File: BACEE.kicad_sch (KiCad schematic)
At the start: 0 parts

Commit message: Created new child sheet, added project symbols
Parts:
- added BT1: Battery, symbol Device:Battery
- added C1, C2: C, symbol Device:C
- added C3, C4: C_Polarized, symbol Device:C_Polarized
- added D1: LED, symbol Device:LED
- added R1, R2: R, symbol Device:R
- added U1: 24LC1025, symbol Memory_EEPROM:24LC1025
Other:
- added sheet Connector (Connectors.kicad_sch)

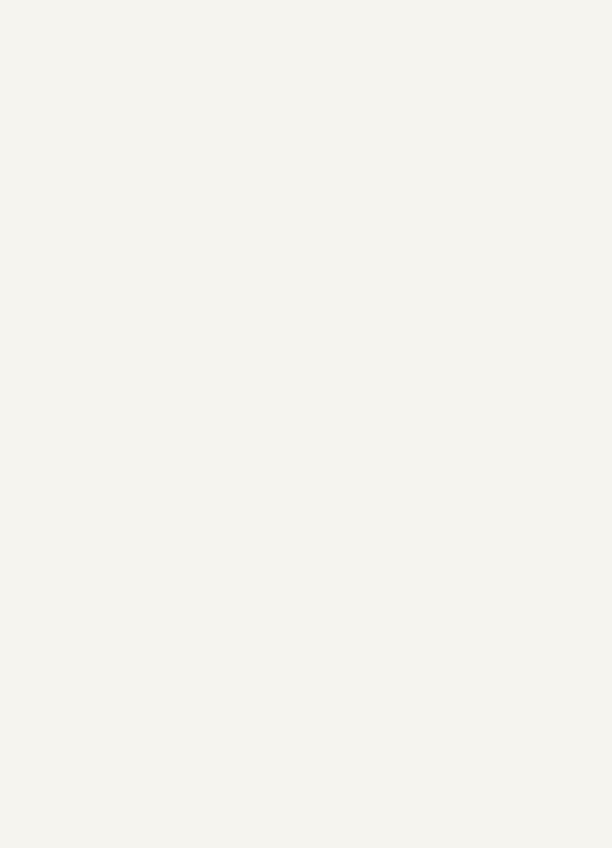
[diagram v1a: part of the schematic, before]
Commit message: Added symbol for ATMEGA328P-AU
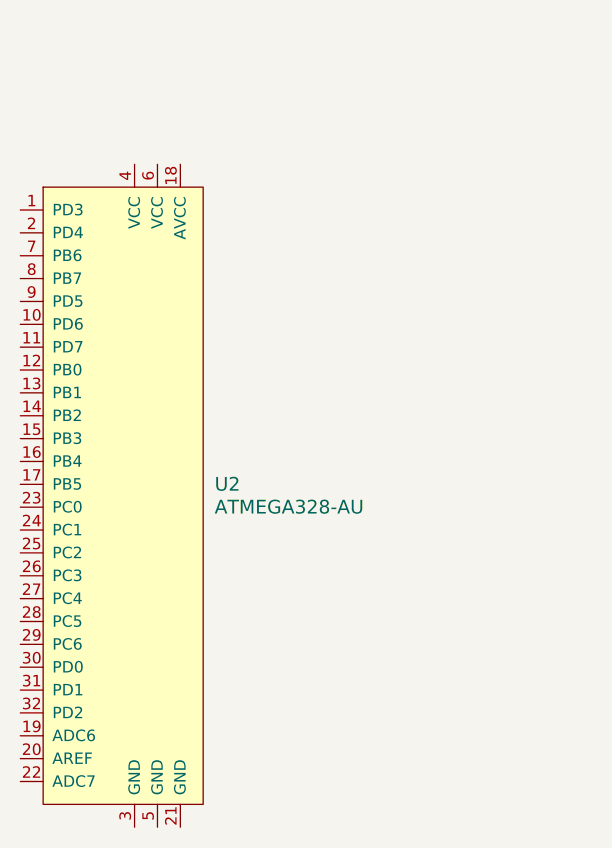
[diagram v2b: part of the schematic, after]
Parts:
- added U2: ATMEGA328-AU, digikey-footprints:TQFP-32_7x7mm, symbol dk_Embedded-Microcontrollers:ATMEGA328-AU
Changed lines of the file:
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@@
+	)
+	(symbol
+		(lib_id "dk_Embedded-Microcontrollers:ATMEGA328-AU")
+		(at 76.2 127 0)
+		(unit 1)
+		(exclude_from_sim no)
+		(in_bom yes)
+		(on_board yes)
+		(dnp no)
+		(fields_autoplaced yes)
+		(property "Reference" "U2"
+			(at 85.09 147.3199 0)
+			(effects
+				(font
+					(size 1.524 1.524)
+				)
+				(justify left)
+			)
+		)
+		(property "Value" "ATMEGA328-AU"
+			(at 85.09 149.8599 0)
+			(effects
+				(font
+					(size 1.524 1.524)
+				)
+				(justify left)
+			)
+		)
+		(property "Footprint" "digikey-footprints:TQFP-32_7x7mm"
+			(at 81.28 121.92 0)
+			(effects
+				(font
+					(size 1.524 1.524)
+				)
+				(justify left)
+				(hide yes)
+			)
+		)
+		(property "Datasheet" "http://www.microchip.com/mymicrochip/filehandler.aspx?ddocname=en608326"
+			(at 81.28 119.38 0)
+			(effects
+				(font
+					(size 1.524 1.524)
+				)
+				(justify left)
+				(hide yes)
+			)
+		)
+		(property "Description" "IC MCU 8BIT 32KB FLASH 32TQFP"
+			(at 76.2 127 0)
+			(effects
+				(font
+					(size 1.27 1.27)
+				)
+				(hide yes)
+			)
+		)
+		(property "Digi-Key_PN" "ATMEGA328-AU-ND"
+			(at 81.28 116.84 0)
+			(effects
+				(font
+					(size 1.524 1.524)
+				)
+				(justify left)
+				(hide yes)
+			)
+		)
+		(property "MPN" "ATMEGA328-AU"
+			(at 81.28 114.3 0)
+			(effects
+				(font
+					(size 1.524 1.524)
+				)
+				(justify left)
+				(hide yes)
+			)
+		)
+		(property "Category" "Integrated Circuits (ICs)"
+			(at 81.28 111.76 0)
+			(effects
+				(font
+					(size 1.524 1.524)
+				)
+				(justify left)
+				(hide yes)
+			)
+		)
+		(property "Family" "Embedded - Microcontrollers"
+			(at 81.28 109.22 0)
+			(effects
+				(font
+					(size 1.524 1.524)
+				)
+				(justify left)
+				(hide yes)
+			)
+		)
+		(property "DK_Datasheet_Link" "http://www.microchip.com/mymicrochip/filehandler.aspx?ddocname=en608326"
+			(at 81.28 106.68 0)
+			(effects
+				(font
+					(size 1.524 1.524)
+				)
+				(justify left)
+				(hide yes)
+			)
+		)
+		(property "DK_Detail_Page" "/product-detail/en/microchip-technology/ATMEGA328-AU/ATMEGA328-AU-ND/2271029"
+			(at 81.28 104.14 0)
+			(effects
+				(font
+					(size 1.524 1.524)
+				)
+				(justify left)
+				(hide yes)
+			)
+		)
+		(property "Description_1" "IC MCU 8BIT 32KB FLASH 32TQFP"
+			(at 81.28 101.6 0)
+			(effects
+				(font
+					(size 1.524 1.524)
+				)
+				(justify left)
+				(hide yes)
+			)
+		)
+		(property "Manufacturer" "Microchip Technology"
+			(at 81.28 99.06 0)
+			(effects
+				(font
+					(size 1.524 1.524)
+				)
+				(justify left)
+				(hide yes)
+			)
+		)
+		(property "Status" "Active"
+			(at 81.28 96.52 0)
+			(effects
+				(font
+					(size 1.524 1.524)
+				)
+				(justify left)
+				(hide yes)
+			)
+		)
+		(pin "15"
+		)
+		(pin "2"
+		)
+		(pin "8"
+		)
+		(pin "25"
+		)
+		(pin "21"
+		)
+		(pin "11"
+		)
+		(pin "9"
+		)
+		(pin "14"
+		)
+		(pin "13"
+		)
+		(pin "12"
+		)
+		(pin "27"
+		)
+		(pin "20"
+		)
+		(pin "17"
+		)
+		(pin "16"
+		)
+		(pin "30"
+		)
+		(pin "22"
+		)
+		(pin "6"
+		)
+		(pin "5"
+		)
+		(pin "23"
+		)
+		(pin "28"
+		)
+		(pin "31"
+		)
+		(pin "32"
+		)
+		(pin "4"
+		)
+		(pin "19"
+		)
+		(pin "10"
+		)
+		(pin "29"
+		)
+		(pin "7"
+		)
+		(pin "26"
+		)
+		(pin "18"
+		)
+		(pin "24"
+		)
+		(pin "1"
+		)
+		(pin "3"
+		)
+		(instances
+			(project ""
+				(path "/6ce24059-c414-47b5-8b66-25e9f97a79bc"
+					(reference "U2")
+					(unit 1)
+				)
+			)
+		)
 	)
 	(symbol

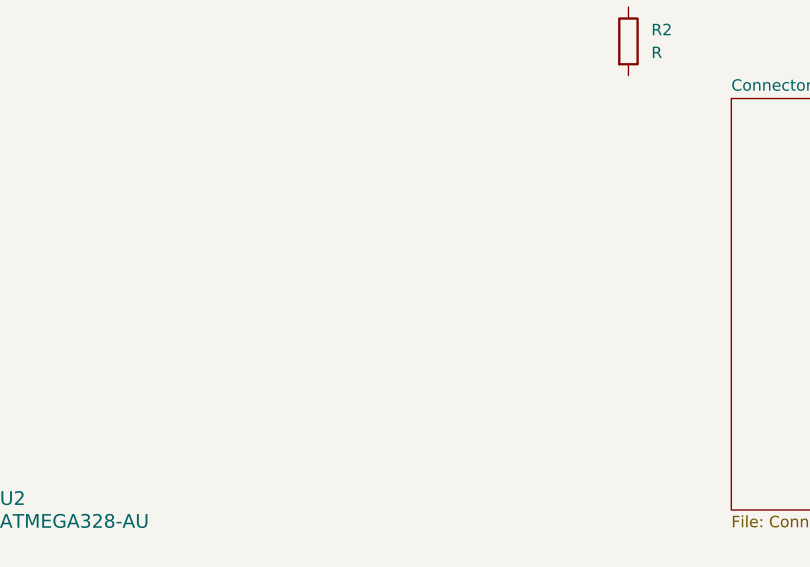
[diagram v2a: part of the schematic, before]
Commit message: Added custom clock IC symbol
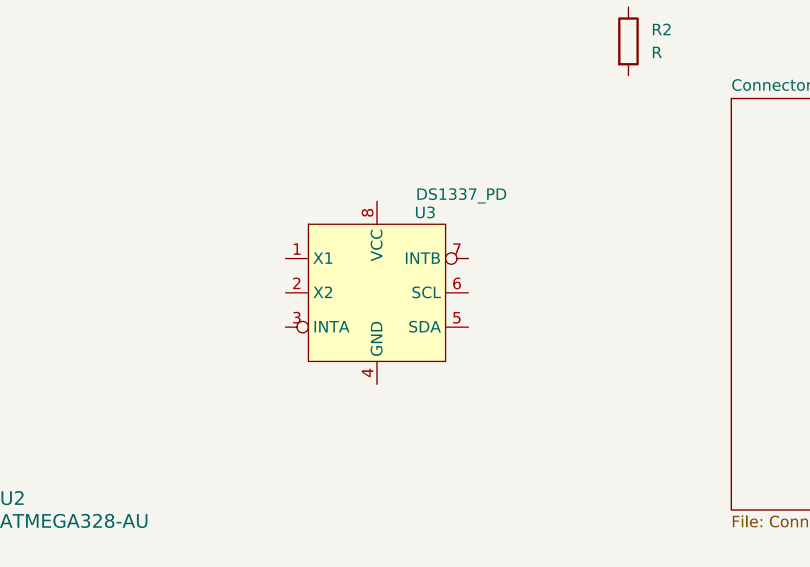
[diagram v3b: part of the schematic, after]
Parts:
- added U3: DS1337_PD, symbol Gathonjia:DS1337_PD
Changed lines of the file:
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@@
+	)
+	(symbol
+		(lib_id "Gathonjia:DS1337_PD")
+		(at 127 124.46 0)
+		(unit 1)
+		(exclude_from_sim no)
+		(in_bom yes)
+		(on_board yes)
+		(dnp no)
+		(property "Reference" "U3"
+			(at 131.1753 115.57 0)
+			(effects
+				(font
+					(size 1.27 1.27)
+				)
+				(justify left)
+			)
+		)
+		(property "Value" "DS1337_PD"
+			(at 131.318 113.538 0)
+			(effects
+				(font
+					(size 1.27 1.27)
+				)
+				(justify left)
+			)
+		)
+		(property "Footprint" ""
+			(at 127 124.46 0)
+			(effects
+				(font
+					(size 1.27 1.27)
+				)
+				(hide yes)
+			)
+		)
+		(property "Datasheet" ""
+			(at 127 124.46 0)
+			(effects
+				(font
+					(size 1.27 1.27)
+				)
+				(hide yes)
+			)
+		)
+		(property "Description" ""
+			(at 127 124.46 0)
+			(effects
+				(font
+					(size 1.27 1.27)
+				)
+				(hide yes)
+			)
+		)
+		(pin "3"
+		)
+		(pin "5"
+		)
+		(pin "8"
+		)
+		(pin "4"
+		)
+		(pin "2"
+		)
+		(pin "1"
+		)
+		(pin "7"
+		)
+		(pin "6"
+		)
+		(instances
+			(project ""
+				(path "/6ce24059-c414-47b5-8b66-25e9f97a79bc"
+					(reference "U3")
+					(unit 1)
+				)
+			)
+		)
 	)
 	(symbol

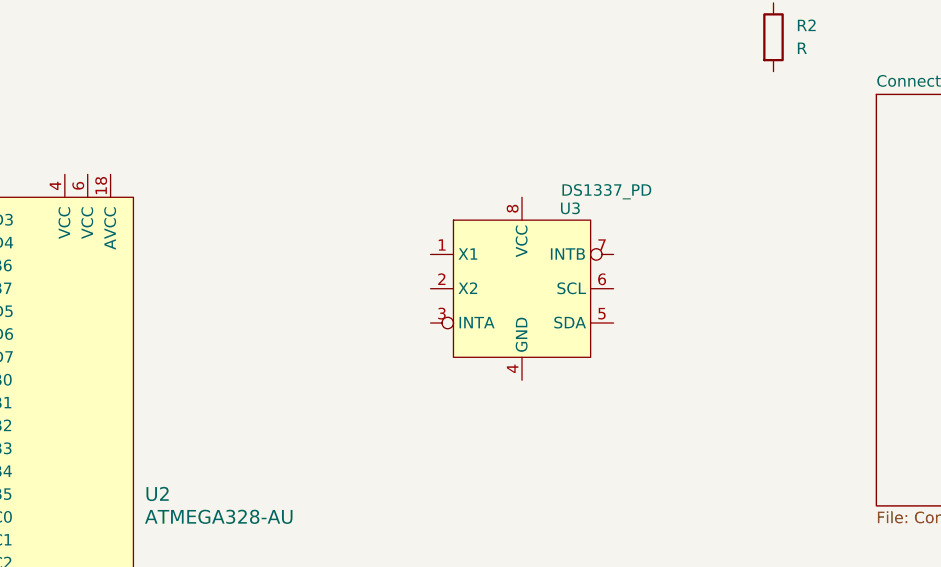
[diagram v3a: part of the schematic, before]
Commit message: Added missing crystals
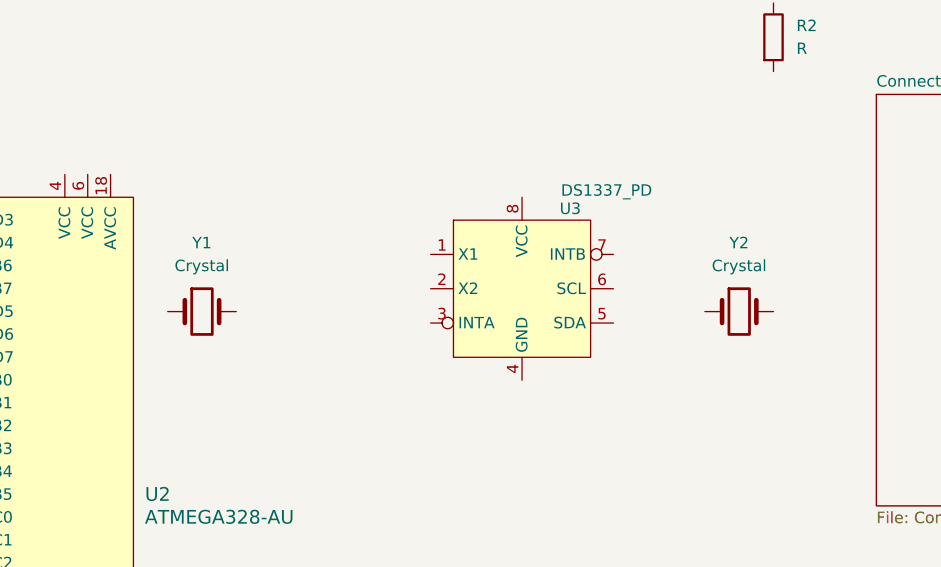
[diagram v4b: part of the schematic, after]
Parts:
- added Y1, Y2: Crystal, symbol Device:Crystal
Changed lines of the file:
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@@
+	)
+	(symbol
+		(lib_id "Device:Crystal")
+		(at 151.13 127 0)
+		(unit 1)
+		(exclude_from_sim no)
+		(in_bom yes)
+		(on_board yes)
+		(dnp no)
+		(fields_autoplaced yes)
+		(property "Reference" "Y2"
+			(at 151.13 119.38 0)
+			(effects
+				(font
+					(size 1.27 1.27)
+				)
+			)
+		)
+		(property "Value" "Crystal"
+			(at 151.13 121.92 0)
+			(effects
+				(font
+					(size 1.27 1.27)
+				)
+			)
+		)
+		(property "Footprint" ""
+			(at 151.13 127 0)
+			(effects
+				(font
+					(size 1.27 1.27)
+				)
+				(hide yes)
+			)
+		)
+		(property "Datasheet" "~"
+			(at 151.13 127 0)
+			(effects
+				(font
+					(size 1.27 1.27)
+				)
+				(hide yes)
+			)
+		)
+		(property "Description" "Two pin crystal"
+			(at 151.13 127 0)
+			(effects
+				(font
+					(size 1.27 1.27)
+				)
+				(hide yes)
+			)
+		)
+		(pin "2"
+		)
+		(pin "1"
+		)
+		(instances
+			(project "BACEE"
+				(path "/6ce24059-c414-47b5-8b66-25e9f97a79bc"
+					(reference "Y2")
+					(unit 1)
+				)
+			)
+		)
 	)
 	(symbol
@@
 					(unit 1)
 				)
+			)
+		)
+	)
+	(symbol
+		(lib_id "Device:Crystal")
+		(at 91.44 127 0)
+		(unit 1)
+		(exclude_from_sim no)
+		(in_bom yes)
+		(on_board yes)
+		(dnp no)
+		(fields_autoplaced yes)
+		(property "Reference" "Y1"
+			(at 91.44 119.38 0)
+			(effects
+				(font
+					(size 1.27 1.27)
+				)
+			)
+		)
+		(property "Value" "Crystal"
+			(at 91.44 121.92 0)
+			(effects
+				(font
+					(size 1.27 1.27)
+				)
+			)
+		)
+		(property "Footprint" ""
+			(at 91.44 127 0)
+			(effects
+				(font
+					(size 1.27 1.27)
+				)
+				(hide yes)
+			)
+		)
+		(property "Datasheet" "~"
+			(at 91.44 127 0)
+			(effects
+				(font
+					(size 1.27 1.27)
+				)
+				(hide yes)
+			)
+		)
+		(property "Description" "Two pin crystal"
+			(at 91.44 127 0)
+			(effects
+				(font
+					(size 1.27 1.27)
+				)
+				(hide yes)
+			)
+		)
+		(pin "2"
+		)
+		(pin "1"
+		)
+		(instances
+			(project ""
+				(path "/6ce24059-c414-47b5-8b66-25e9f97a79bc"
+					(reference "Y1")
+					(unit 1)
+				)

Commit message: Arranged symbols
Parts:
- removed C4: C_Polarized, symbol Device:C_Polarized
- added U4: 24LC1025, symbol Memory_EEPROM:24LC1025
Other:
- moved on the sheet: BT1, C1, C2, C3, D1, R1, R2, U1, U2, U3, Y1, Y2

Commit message: Assigned the footprints
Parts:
- BT1: footprint (none) -> Connector_PinHeader_2.54mm:PinHeader_1x02_P2.54mm_Vertical
- C1, C2, C3: footprint (none) -> Capacitor_SMD:C_0805_2012Metric_Pad1.18x1.45mm_HandSolder
- D1: footprint (none) -> LED_SMD:LED_0805_2012Metric_Pad1.15x1.40mm_HandSolder
- R1, R2: footprint (none) -> Resistor_SMD:R_0805_2012Metric_Pad1.20x1.40mm_HandSolder
- U1: footprint (none) -> Package_SO:SOIC-8_5.3x5.3mm_P1.27mm
- U2: renamed from U4; footprint (none) -> Package_SO:SOIC-8_5.3x5.3mm_P1.27mm
- U3: footprint (none) -> Package_SO:SOIC-8_3.9x4.9mm_P1.27mm
- Y1: footprint (none) -> Crystal:Crystal_SMD_MicroCrystal_CC7V-T1A-2Pin_3.2x1.5mm
- Y2: footprint (none) -> Crystal:Crystal_SMD_5032-2Pin_5.0x3.2mm_HandSoldering
- renumbered U2 to U4
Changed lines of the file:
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@@
 		(dnp no)
 		(fields_autoplaced yes)
-		(property "Reference" "U2"
+		(property "Reference" "U4"
 			(at 184.15 88.8999 0)
 			(effects
@@
 			(project ""
 				(path "/6ce24059-c414-47b5-8b66-25e9f97a79bc"
-					(reference "U2")
+					(reference "U4")
 					(unit 1)
 				)
@@
 			)
 		)
-		(property "Footprint" ""
+		(property "Footprint" "Connector_PinHeader_2.54mm:PinHeader_1x02_P2.54mm_Vertical"
 			(at 215.9 68.326 90)
 			(effects
@@
 			)
 		)
-		(property "Footprint" ""
+		(property "Footprint" "Capacitor_SMD:C_0805_2012Metric_Pad1.18x1.45mm_HandSolder"
 			(at 110.1852 69.85 0)
 			(effects
@@
 			)
 		)
-		(property "Footprint" ""
+		(property "Footprint" "Resistor_SMD:R_0805_2012Metric_Pad1.20x1.40mm_HandSolder"
 			(at 140.462 109.22 90)
 			(effects
@@
 			)
 		)
-		(property "Footprint" ""
+		(property "Footprint" "LED_SMD:LED_0805_2012Metric_Pad1.15x1.40mm_HandSolder"
 			(at 140.97 83.82 0)
 			(effects
@@
 			)
 		)
-		(property "Footprint" ""
+		(property "Footprint" "Crystal:Crystal_SMD_5032-2Pin_5.0x3.2mm_HandSoldering"
 			(at 135.89 66.04 0)
 			(effects
@@
 			)
 		)
-		(property "Footprint" ""
+		(property "Footprint" "Capacitor_SMD:C_0805_2012Metric_Pad1.18x1.45mm_HandSolder"
 			(at 110.1852 82.55 0)
 			(effects
@@
 			)
 		)
-		(property "Footprint" ""
+		(property "Footprint" "Resistor_SMD:R_0805_2012Metric_Pad1.20x1.40mm_HandSolder"
 			(at 123.952 92.71 90)
 			(effects
@@
 			)
 		)
-		(property "Footprint" ""
+		(property "Footprint" "Crystal:Crystal_SMD_MicroCrystal_CC7V-T1A-2Pin_3.2x1.5mm"
 			(at 26.67 73.66 0)
 			(effects
@@
 		(dnp no)
 		(fields_autoplaced yes)
-		(property "Reference" "U4"
+		(property "Reference" "U2"
 			(at 68.1833 165.1 0)
 			(effects
@@
 			)
 		)
-		(property "Footprint" ""
+		(property "Footprint" "Package_SO:SOIC-8_5.3x5.3mm_P1.27mm"
 			(at 66.04 175.26 0)
 			(effects
@@
 			(project "BACEE"
 				(path "/6ce24059-c414-47b5-8b66-25e9f97a79bc"
-					(reference "U4")
+					(reference "U2")
 					(unit 1)
 				)
@@
 			)
 		)
-		(property "Footprint" ""
+		(property "Footprint" "Capacitor_SMD:C_0805_2012Metric_Pad1.18x1.45mm_HandSolder"
 			(at 229.5652 90.17 0)
 			(effects
@@
 			)
 		)
-		(property "Footprint" ""
+		(property "Footprint" "Package_SO:SOIC-8_5.3x5.3mm_P1.27mm"
 			(at 64.77 149.86 0)
 			(effects
@@
 			)
 		)
-		(property "Footprint" ""
+		(property "Footprint" "Package_SO:SOIC-8_3.9x4.9mm_P1.27mm"
 			(at 49.53 77.47 0)
 			(effects

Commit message: Completed adding components values
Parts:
- BT1: value Battery -> Battery 3V
- C1, C2: value C -> 22pF
- C3: value C_Polarized -> 10uF
- R1: value R -> 330Ohm
- R2: value R -> 10KOhm
- U3: value DS1337_PD -> DS13375+
- Y1: value Crystal -> 32MHz
- Y2: value Crystal -> 16MHz
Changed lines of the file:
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@@
 			)
 		)
-		(property "Value" "Battery"
+		(property "Value" "Battery 3V"
 			(at 219.71 70.5484 0)
 			(effects
@@
 			)
 		)
-		(property "Value" "C"
+		(property "Value" "22pF"
 			(at 113.03 67.3099 0)
 			(effects
@@
 			)
 		)
-		(property "Value" "R"
+		(property "Value" "10KOhm"
 			(at 144.78 110.4899 0)
 			(effects
@@
 			)
 		)
-		(property "Value" "Crystal"
+		(property "Value" "16MHz"
 			(at 135.89 60.96 0)
 			(effects
@@
 			)
 		)
-		(property "Value" "C"
+		(property "Value" "22pF"
 			(at 113.03 80.0099 0)
 			(effects
@@
 			)
 		)
-		(property "Value" "R"
+		(property "Value" "330Ohm"
 			(at 128.27 93.9799 0)
 			(effects
@@
 			)
 		)
-		(property "Value" "Crystal"
+		(property "Value" "32MHz"
 			(at 26.67 68.58 0)
 			(effects
@@
 			)
 		)
-		(property "Value" "C_Polarized"
+		(property "Value" "10uF"
 			(at 232.41 86.7409 0)
 			(effects
@@
 			)
 		)
-		(property "Value" "DS1337_PD"
+		(property "Value" "DS13375+"
 			(at 53.848 66.548 0)
 			(effects

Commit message: Completed wiring in child sheet
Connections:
- net GND: now also U4.21 (GND), U4.3 (GND), U4.5 (GND)
- net D3: now reaches U4.1 (PD3)
- net D6: now reaches U4.10 (PD6)
- net D7: now reaches U4.11 (PD7)
- net D8: now reaches U4.12 (PB0)
- net MOSI: now reaches U4.15 (PB3)
- net MISO: now reaches U4.16 (PB4)
- net SCK: now reaches U4.17 (PB5)
- net VCC: now reaches U4.18 (AVCC)
- net VCC: now also U4.4 (VCC), U4.6 (VCC)
- net D4: now reaches U4.2 (PD4)
- net SDA: now reaches U4.27 (PC4)
- net RESET: now reaches U4.29 (PC6)
- net RX: now reaches U4.30 (PD0)
- net TX: now reaches U4.31 (PD1)
- net D2: now reaches U4.32 (PD2)
- net D5: now reaches U4.9 (PD5)
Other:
- sheet Connector ports: added D2, D3, D4, D5, D6, D7, D8, GND, MISO, MOSI, RESET, RX, SCK, SDA, TX, VCC; removed none
